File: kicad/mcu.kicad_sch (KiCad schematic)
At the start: 20 parts, among them J2 GPIO Breakout, J3 SWD Debug, SW2 SW_Push, U3 RP2040

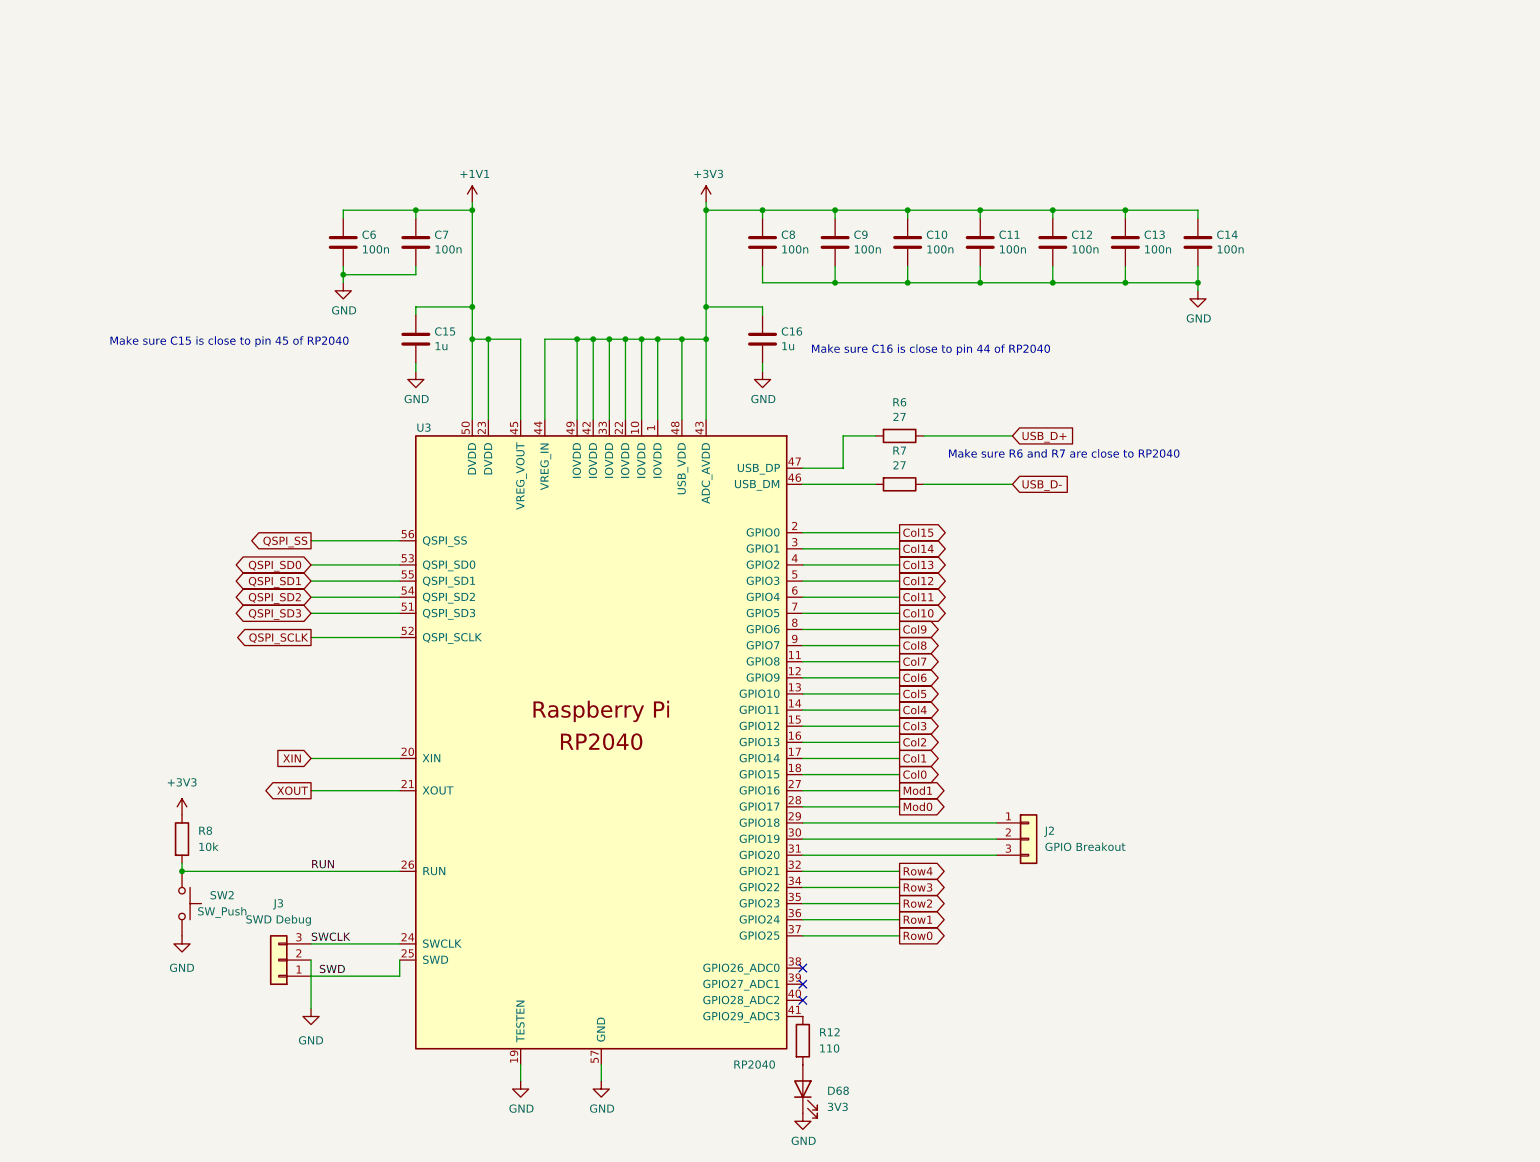
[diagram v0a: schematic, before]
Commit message: actual attempt at source controlling kicad project
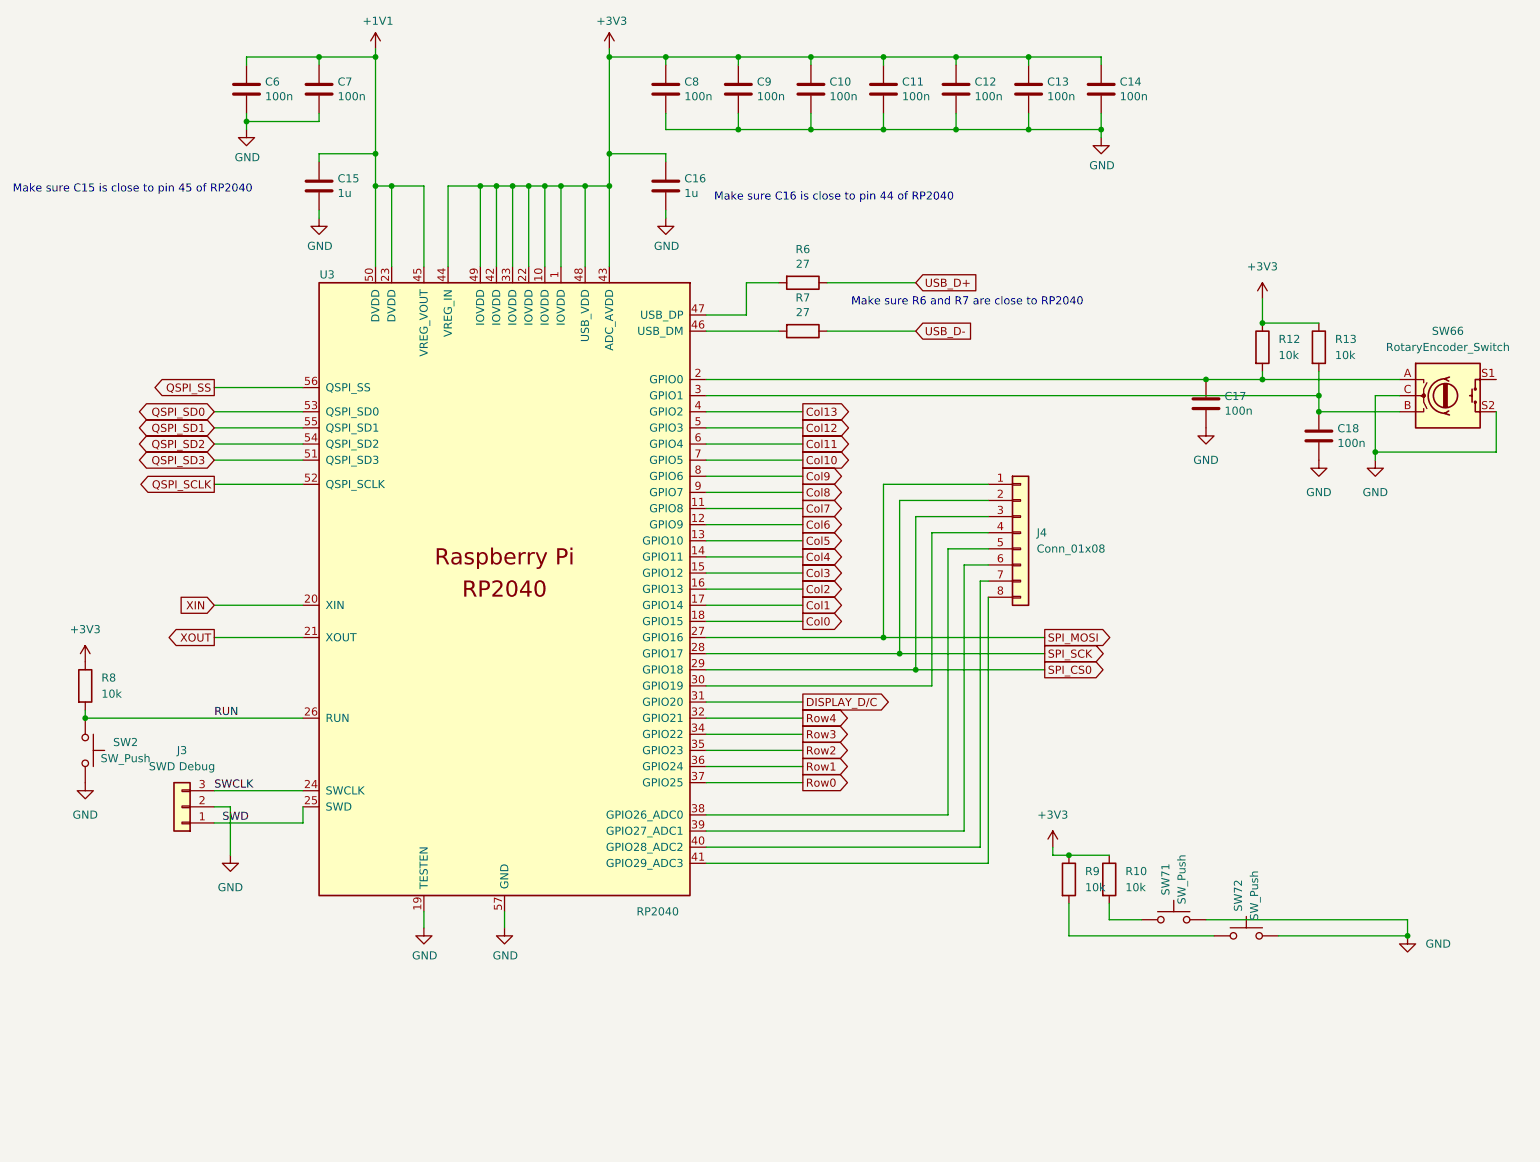
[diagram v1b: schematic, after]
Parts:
- removed D68: 3V3, LED_SMD:LED_0603_1608Metric, symbol Device:LED
- removed J2: GPIO Breakout, Connector_PinHeader_2.54mm:PinHeader_1x03_P2.54mm_Vertical, symbol Connector_Generic:Conn_01x03
- added C17, C18: 100n, Capacitor_SMD:C_0603_1608Metric, symbol Device:C
- added J4: Conn_01x08, symbol Connector_Generic:Conn_01x08
- added R10, R13, R9: 10k, Resistor_SMD:R_0603_1608Metric, symbol Device:R
- added SW66: RotaryEncoder_Switch, symbol Device:RotaryEncoder_Switch
- added SW71, SW72: SW_Push, Button_Switch_SMD:SW_Push_1P1T_NO_CK_KMR2, symbol Switch:SW_Push
- R12: value 110 -> 10k
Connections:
- net Col15 is gone; now on an unnamed net: U3.2 (GPIO0)
- net +3V3: now also R12.1, R10.1, R13.1, R9.1
- net GND: now also C17.2, C18.2, SW66.C, SW66.S2, SW71.2, SW72.2
- net at U3.41 (GPIO29_ADC3): now also J4.8 (Pin_8); no longer R12.1
- net at R12.2: now also C17.1, SW66.A
- net SPI_CS0: now reaches U3.29 (GPIO18)
- net SPI_CS0: now also J4.3 (Pin_3)
- net at U3.30 (GPIO19): now also J4.4 (Pin_4)
- net DISPLAY_D/C: now reaches U3.31 (GPIO20)
- net at U3.38 (GPIO26_ADC0): now also J4.5 (Pin_5)
- net at U3.39 (GPIO27_ADC1): now also J4.6 (Pin_6)
- net at U3.40 (GPIO28_ADC2): now also J4.7 (Pin_7)
- net Col14: no longer names the net of U3.3 (GPIO1)
- net Col14: now also C18.1, R13.2, SW66.B
- net Mod0 renamed SPI_SCK
- net SPI_SCK: now also J4.2 (Pin_2)
- net Mod1 renamed SPI_MOSI
- net SPI_MOSI: now also J4.1 (Pin_1)
- new net: R9.2, SW72.1
- new net: R10.2, SW71.1
- no-connect marks 3 -> 0
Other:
- moved on the sheet: C10, C11, C12, C13, C14, C15, C16, C6, C7, C8, C9, J3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

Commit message: moving things around
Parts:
- J2: renamed from J4; footprint (none) -> Connector_PinSocket_2.54mm:PinSocket_2x04_P2.54mm_Horizontal
- SW2: renamed from SW66; footprint (none) -> Rotary_Encoder:RotaryEncoder_Alps_EC11E-Switch_Vertical_H20mm_MountingHoles
- SW4: renamed from SW71; footprint Button_Switch_SMD:SW_Push_1P1T_NO_CK_KMR2 -> Button_Switch_THT:SW_Push_2P1T_Toggle_CK_PVA1xxH3xxxxxxV2
- SW5: renamed from SW72; footprint Button_Switch_SMD:SW_Push_1P1T_NO_CK_KMR2 -> Button_Switch_THT:SW_Push_2P1T_Toggle_CK_PVA1xxH2xxxxxxV2
- renumbered R13 to R10, R8 to R11, R9 to R12, R10 to R13, R6 to R7, R7 to R8, R12 to R9, SW2 to SW3
